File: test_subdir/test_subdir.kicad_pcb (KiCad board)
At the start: 4 copper layers, 49.8 x 48.2 mm, 12 parts, among them J1 Conn_01x08_Male, J2 Conn_01x08_Male, J3 Conn_01x08_Male, J4 USB_B, J5 Conn_01x08_Male, J6 Conn_01x06_Male, U1 FT2232H, Y1 12 MHz

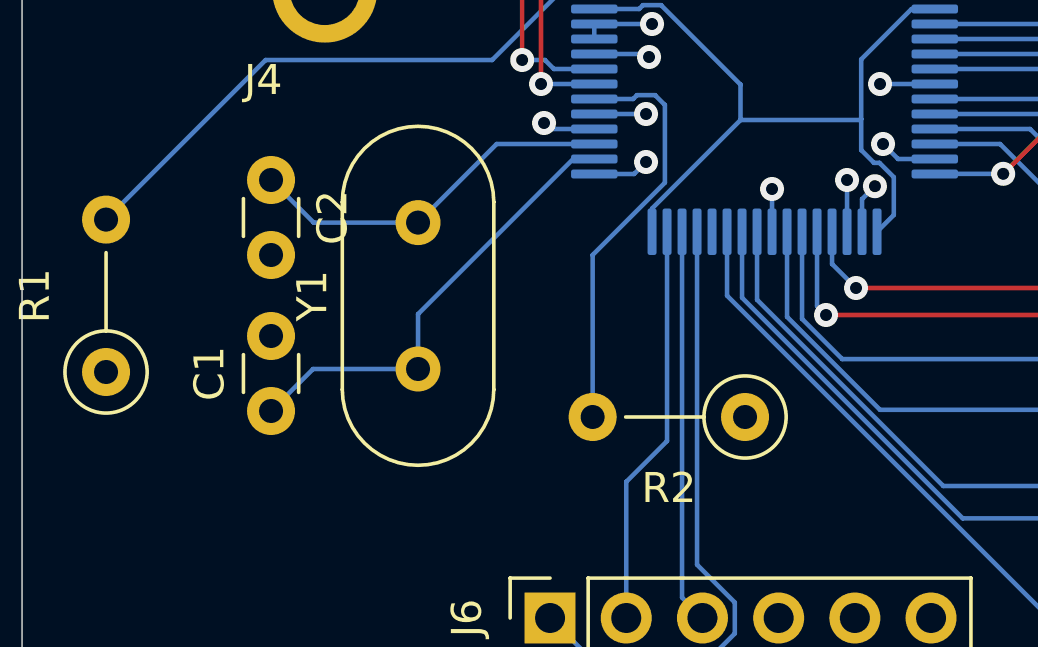
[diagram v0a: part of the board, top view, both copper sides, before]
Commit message: Migrated the sub-dir example to KiCad 6.0.11
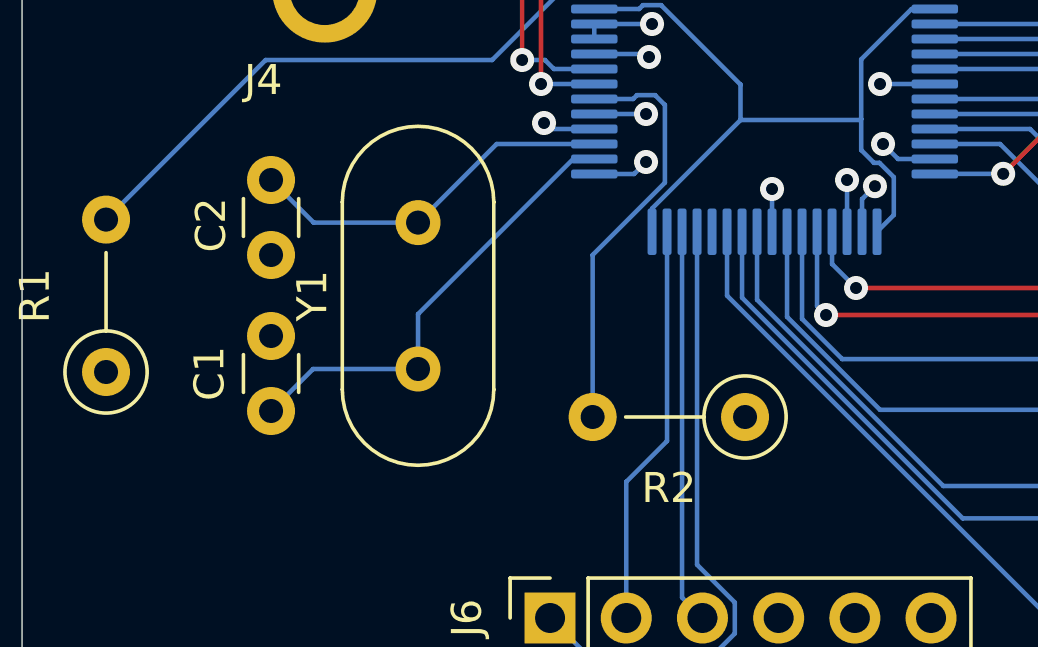
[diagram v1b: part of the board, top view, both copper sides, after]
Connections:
- net +3V3 renamed +3.3V
- U1 pad 36: Net-(U1-Pad36) -> unconnected-(U1-Pad36)
- U1 pad 60: Net-(U1-Pad60) -> unconnected-(U1-Pad60)
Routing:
- added copper zone on In1.Cu, net GND
- removed copper zone on GND.Cu, net GND
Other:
- net class Default removed

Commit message: Migrated the sub-dir example to KiCad 7.0.11
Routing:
- net +5V: track 60.0 -> 62.0 mm
